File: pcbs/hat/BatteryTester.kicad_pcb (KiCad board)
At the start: 2 copper layers, 150 parts, among them J1 Screw_Terminal_01x02, J2 XT60, J3 XT60, J4 XT60, J5 XT60, J6 XT60, J7 XT60, J8 XT60, J9 XT60, Q1 Q_NMOS_DGS, Q10 Q_NMOS_DGS, Q11 Q_NMOS_DGS, Q12 Q_NMOS_DGS, Q13 Q_NMOS_DGS, Q14 Q_NMOS_DGS, Q15 Q_NMOS_DGS, Q16 Q_NMOS_DGS, Q2 Q_NMOS_DGS, Q3 Q_NMOS_DGS, Q4 Q_NMOS_DGS, Q5 Q_NMOS_DGS, Q6 Q_NMOS_DGS, Q7 Q_NMOS_DGS, Q8 Q_NMOS_DGS, Q9 Q_NMOS_DGS, U1 INA181A4IDBVR, U10 TP5000_Breakout_Akaddy, U11 INA181A4IDBVR, U12 TP5000_Breakout_Akaddy, U13 INA181A4IDBVR, U14 TP5000_Breakout_Akaddy, U15 INA181A4IDBVR, U16 TP5000_Breakout_Akaddy, U17 NUCLEO-F401RE, U18 MCP3008, U19 MCP3008, U2 TP5000_Breakout_Akaddy, U20 MCP3008, U21 ???, U3 INA181A4IDBVR, U4 TP5000_Breakout_Akaddy, U5 INA181A4IDBVR, U6 TP5000_Breakout_Akaddy, U7 INA181A4IDBVR, U8 TP5000_Breakout_Akaddy, U9 INA181A4IDBVR

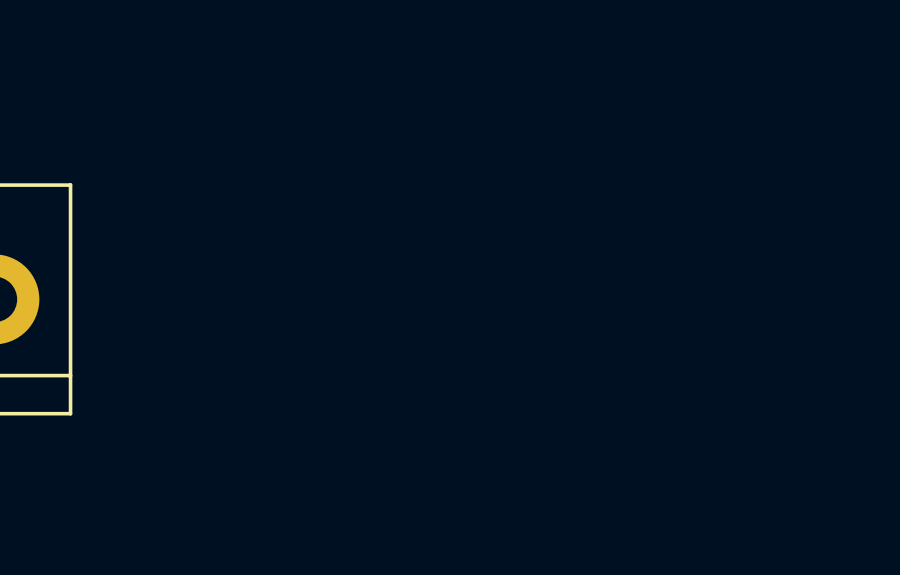
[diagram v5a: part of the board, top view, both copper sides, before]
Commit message: fix the current sensor
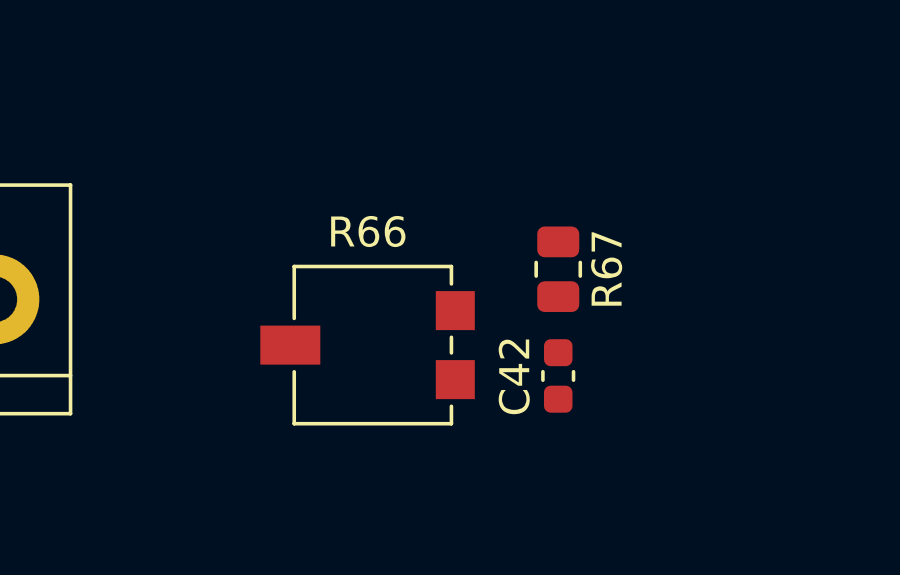
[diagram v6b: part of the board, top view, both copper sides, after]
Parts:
- added C42: 1u, Capacitor_SMD:C_0603_1608Metric, F.Cu at (80.3, 115.3)
- added R66: TS53YL503MR10, Potentiometer_SMD:Potentiometer_Vishay_TS53YL_Vertical, F.Cu at (74.1, 114.3)
- added R67: 25k, Resistor_SMD:R_0805_2012Metric, F.Cu at (80.3, 111.8)
- U1, U11, U13, U15, U3, U5, U7, U9: value INA181A4IDBVR -> INA181A3IDBVR
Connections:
- J2 pad 1: /test-battery-1/VBAT -> /SENSOR_10
- J3 pad 1: /test-battery-2/VBAT -> /SENSOR_20
- J4 pad 1: /test-battery-3/VBAT -> /SENSOR_30
- J5 pad 1: /test-battery-4/VBAT -> /SENSOR_40
- J6 pad 1: /test-battery-5/VBAT -> /SENSOR_50
- J7 pad 1: /test-battery-8/VBAT -> /SENSOR_80
- J8 pad 1: /test-battery-7/VBAT -> /SENSOR_70
- J9 pad 1: /test-battery-6/VBAT -> /SENSOR_60
- R10 pad 2: /test-battery-2/VBAT -> /SENSOR_20
- R18 pad 2: /test-battery-3/VBAT -> /SENSOR_30
- R2 pad 2: /test-battery-1/VBAT -> /SENSOR_10
- R26 pad 2: /test-battery-4/VBAT -> /SENSOR_40
- R34 pad 2: /test-battery-5/VBAT -> /SENSOR_50
- R42 pad 2: /test-battery-8/VBAT -> /SENSOR_80
- R50 pad 2: /test-battery-7/VBAT -> /SENSOR_70
- R58 pad 2: /test-battery-6/VBAT -> /SENSOR_60
- U1 pad 5: GND -> Vref_I_SENS
- U10 pad 3: /test-battery-5/VBAT -> /SENSOR_50
- U11 pad 5: GND -> Vref_I_SENS
- U12 pad 3: /test-battery-8/VBAT -> /SENSOR_80
- U13 pad 5: GND -> Vref_I_SENS
- U14 pad 3: /test-battery-7/VBAT -> /SENSOR_70
- U15 pad 5: GND -> Vref_I_SENS
- U16 pad 3: /test-battery-6/VBAT -> /SENSOR_60
- U2 pad 3: /test-battery-1/VBAT -> /SENSOR_10
- U3 pad 5: GND -> Vref_I_SENS
- U4 pad 3: /test-battery-2/VBAT -> /SENSOR_20
- U5 pad 5: GND -> Vref_I_SENS
- U6 pad 3: /test-battery-3/VBAT -> /SENSOR_30
- U7 pad 5: GND -> Vref_I_SENS
- U8 pad 3: /test-battery-4/VBAT -> /SENSOR_40
- U9 pad 5: GND -> Vref_I_SENS

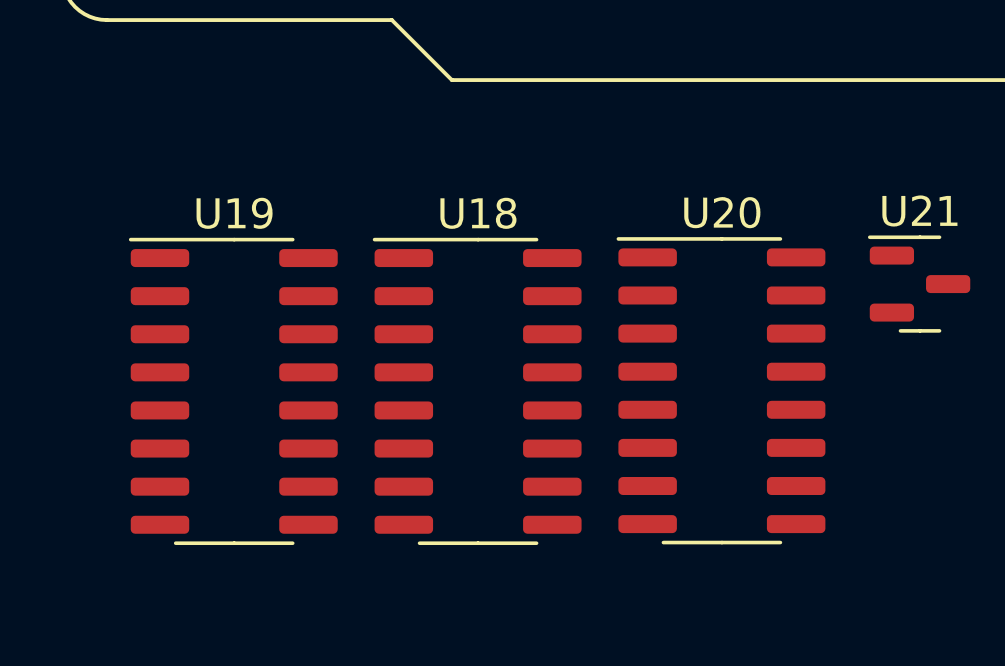
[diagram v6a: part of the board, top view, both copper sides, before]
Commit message: change ADCs and connect all Sensors and Signals
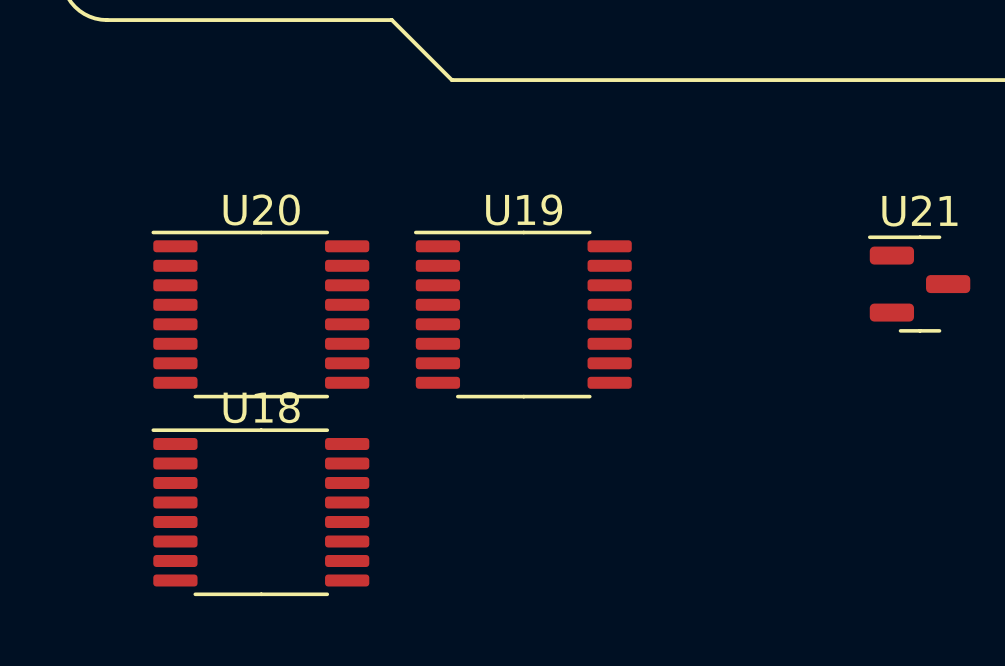
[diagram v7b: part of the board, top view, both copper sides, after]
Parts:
- U18, U19, U20: value MCP3008 -> ADS7828; footprint Package_SO:SOIC-16_3.9x9.9mm_P1.27mm -> Package_SO:TSSOP-16_4.4x5mm_P0.65mm
- moved U20 15.6 mm to (27.8, 110.2)
- moved U19 9.99 mm to (36.6, 110.2)
- moved U18 8.27 mm to (27.8, 116.8)
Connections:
- U17 pad CN10_1: unconnected-(U17-PadCN10_1) -> /SENSOR_43
- U17 pad CN10_13: unconnected-(U17-PadCN10_13) -> /SIGNAL_11
- U17 pad CN10_14: unconnected-(U17-PadCN10_14) -> /SIGNAL_81
- U17 pad CN10_15: unconnected-(U17-PadCN10_15) -> /SIGNAL_21
- U17 pad CN10_16: unconnected-(U17-PadCN10_16) -> /SENSOR_53
- U17 pad CN10_17: unconnected-(U17-PadCN10_17) -> /SIGNAL_30
- U17 pad CN10_19: unconnected-(U17-PadCN10_19) -> /SENSOR_23
- U17 pad CN10_2: unconnected-(U17-PadCN10_2) -> /SENSOR_33
- U17 pad CN10_21: unconnected-(U17-PadCN10_21) -> /SIGNAL_61
- U17 pad CN10_23: unconnected-(U17-PadCN10_23) -> /SIGNAL_51
- U17 pad CN10_24: unconnected-(U17-PadCN10_24) -> /SIGNAL_41
- U17 pad CN10_26: unconnected-(U17-PadCN10_26) -> /SENSOR_83
- U17 pad CN10_27: unconnected-(U17-PadCN10_27) -> /SIGNAL_20
- U17 pad CN10_28: unconnected-(U17-PadCN10_28) -> /SENSOR_73
- U17 pad CN10_29: unconnected-(U17-PadCN10_29) -> /SIGNAL_40
- U17 pad CN10_3: unconnected-(U17-PadCN10_3) -> /Board/SCL
- U17 pad CN10_30: unconnected-(U17-PadCN10_30) -> /SENSOR_63
- U17 pad CN10_33: unconnected-(U17-PadCN10_33) -> /SIGNAL_71
- U17 pad CN10_4: unconnected-(U17-PadCN10_4) -> /SENSOR_13
- U17 pad CN10_5: unconnected-(U17-PadCN10_5) -> /Board/SDA
- U17 pad CN7_1: /SIGNAL_21 -> /SIGNAL_60
- U17 pad CN7_13: /SIGNAL_11 -> unconnected-(U17-PadCN7_13)
- U17 pad CN7_17: unconnected-(U17-PadCN7_17) -> /SIGNAL_80
- U17 pad CN7_2: /SIGNAL_10 -> /SIGNAL_50
- U17 pad CN7_21: unconnected-(U17-PadCN7_21) -> /SIGNAL_10
- U17 pad CN7_3: /SIGNAL_20 -> /SIGNAL_70
- U17 pad CN7_34: unconnected-(U17-PadCN7_34) -> /SIGNAL_31
- U18 pad 10: /Board/SPI_ADC_CS_1 -> +5VA
- U18 pad 11: /Board/SPI_ADC_MOSI -> GND
- U18 pad 12: /Board/SPI_ADC_MISO -> GND
- U18 pad 13: /Board/SPI_ADC_SCK -> GND
- U18 pad 14: GND -> /Board/SCL
- U18 pad 15: +5VA -> /Board/SDA
- U19 pad 10: /Board/SPI_ADC_CS_2 -> +5VA
- U19 pad 11: /Board/SPI_ADC_MOSI -> GND
- U19 pad 12: /Board/SPI_ADC_MISO -> +5V
- U19 pad 13: /Board/SPI_ADC_SCK -> GND
- U19 pad 14: GND -> /Board/SCL
- U19 pad 15: +5VA -> /Board/SDA
- U20 pad 10: /Board/SPI_ADC_CS_3 -> +5VA
- U20 pad 11: /Board/SPI_ADC_MOSI -> GND
- U20 pad 12: /Board/SPI_ADC_MISO -> GND
- U20 pad 13: /Board/SPI_ADC_SCK -> +5V
- U20 pad 14: GND -> /Board/SCL
- U20 pad 15: +5VA -> /Board/SDA
